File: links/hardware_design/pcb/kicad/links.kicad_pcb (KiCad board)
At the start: 2 copper layers, 19 x 108.4 mm, 55 parts, among them IC1 OPA4171, IC2 TL072PW, IC3 LM321MF, IC4 TL072PW, IC5 LM321MF, J1 PJ301_THONKICONN6, J10 PJ301_THONKICONN6, J11 PJ301_THONKICONN6, J12 PJ301_THONKICONN6, J2 PJ301_THONKICONN6, J3 PJ301_THONKICONN6, J4 PJ301_THONKICONN6, J5 PJ301_THONKICONN6, J6 PJ301_THONKICONN6, J7 PJ301_THONKICONN6, J8 PJ301_THONKICONN6, J9 PJ301_THONKICONN6

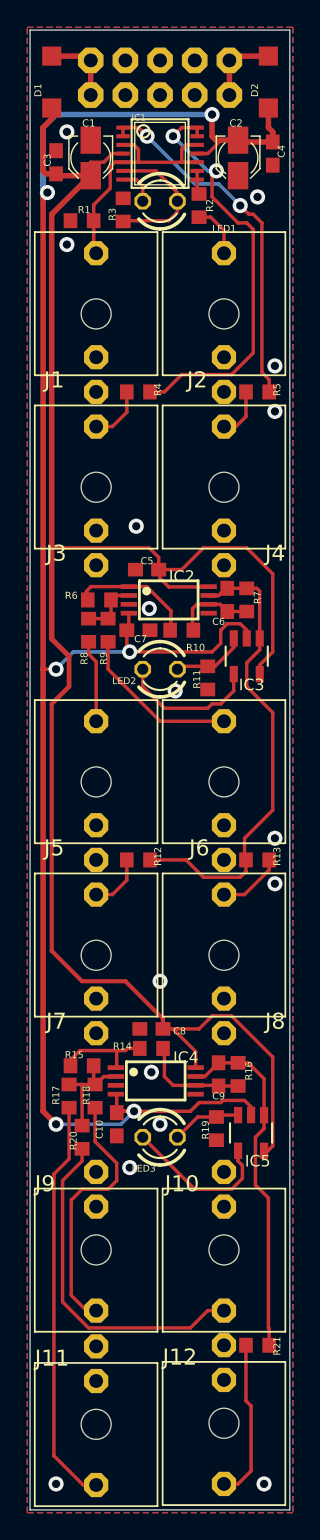
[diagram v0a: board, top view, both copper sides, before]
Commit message: links: move LEDs to left side
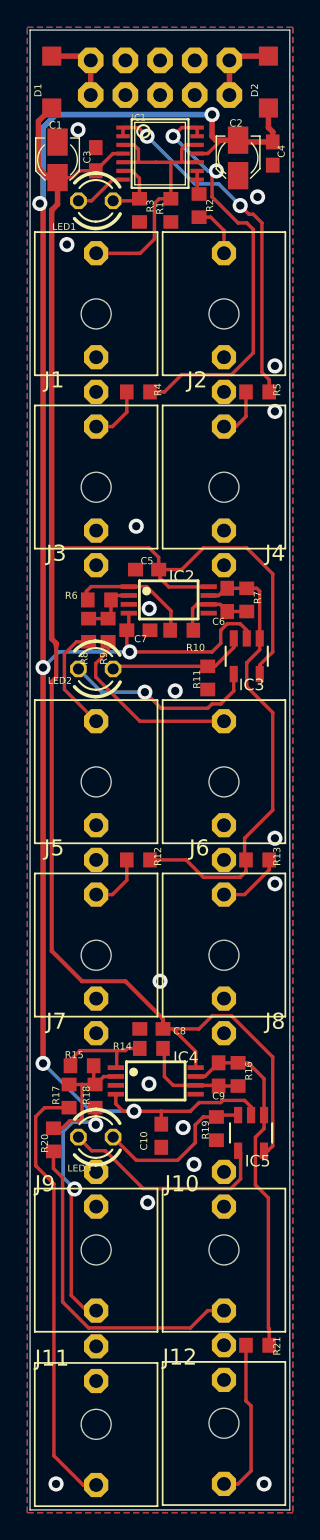
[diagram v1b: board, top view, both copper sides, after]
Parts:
- IC3, IC5: value LM321MF -> LM321?MF
- moved R1 6.55 mm to (149.3, 64.0), turned to 90 degrees
- moved LED1 4.71 mm to (143.8, 63.3)
- moved LED2 4.71 mm to (143.8, 97.6)
- moved LED3 4.71 mm to (143.8, 131.9)
- moved C10 3.37 mm to (148.6, 131.8)
- moved C3 2.92 mm to (143.8, 60.2)
- moved C1 2.44 mm to (141.0, 60.3)
- moved R20 2.10 mm to (140.7, 132.1)
- moved R3 1.19 mm to (147.0, 64.0), turned to -90 degrees
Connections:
- J12 pad P2: (no net) -> unconnected-(J12-2-PadP2)
- J2 pad P2: (no net) -> unconnected-(J2-2-PadP2)
- J3 pad P2: (no net) -> unconnected-(J3-2-PadP2)
- J4 pad P2: (no net) -> unconnected-(J4-2-PadP2)
- J7 pad P2: (no net) -> unconnected-(J7-2-PadP2)
- J8 pad P2: (no net) -> unconnected-(J8-2-PadP2)
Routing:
- net Net-(IC5--IN): track 5.37 -> 12.2 mm
- net Net-(IC1B--IN): track 10.3 -> 4.93 mm
- net Net-(IC3--IN): track 5.46 -> 10.2 mm
- net Net-(IC5-OUT): track 11.4 -> 15.9 mm
- net Net-(IC3-OUT): track 10.4 -> 14.3 mm, vias 0 -> 1
- net VEE: track 140.5 -> 136.6 mm
- net Net-(IC1A-+IN): track 17.9 -> 21.4 mm
- net Net-(J11-3): track 29.9 -> 32.1 mm
- net Net-(J5-3): track 6.05 -> 8.04 mm
- net Net-(IC4A--IN): track 8.48 -> 10.3 mm
- net VCC: track 133.8 -> 132.2 mm
- net Net-(J6-3): track 12.1 -> 13.7 mm
- net Net-(IC1B-OUT): track 2.76 -> 3.91 mm
- net Net-(J10-3): track 24.9 -> 24.4 mm
- net Net-(J9-3): track 19.2 -> 18.8 mm, vias 0 -> 2
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
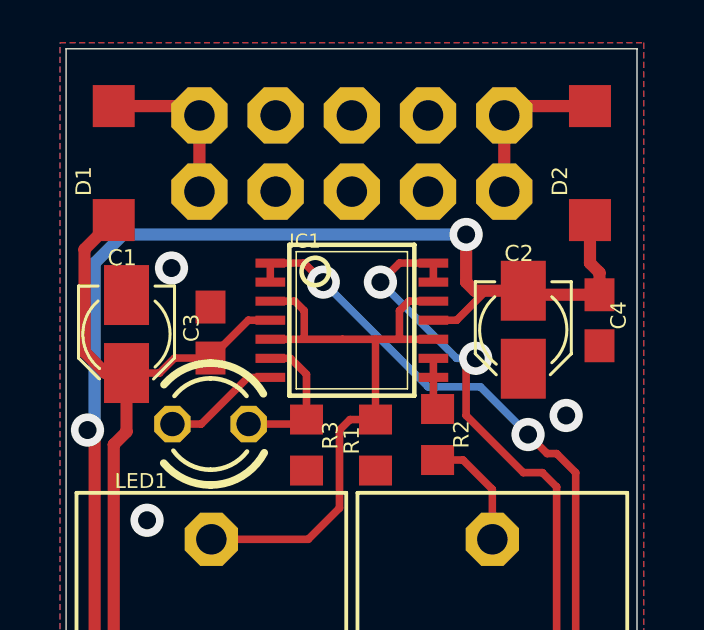
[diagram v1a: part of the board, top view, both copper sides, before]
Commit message: links: change panasonic A to 3x5.3mm footprint
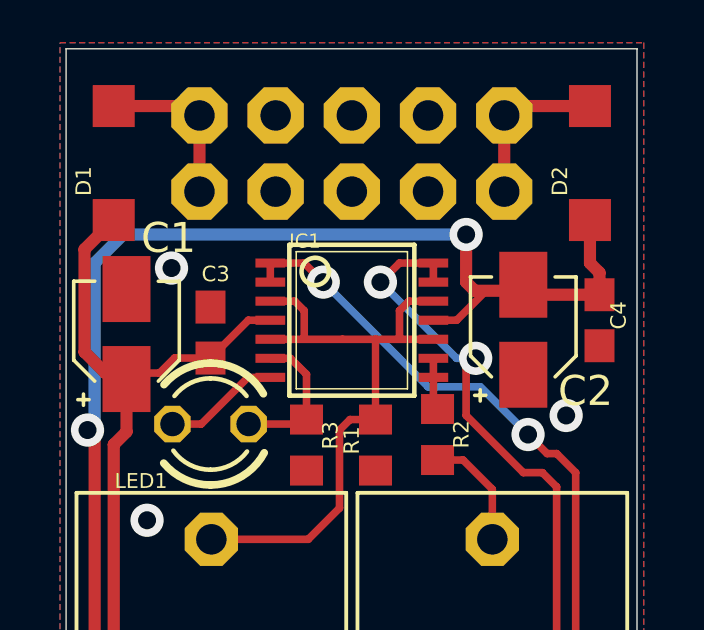
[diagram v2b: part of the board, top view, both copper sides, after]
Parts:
- C1, C2: footprint links:PANASONIC_A -> Capacitor_SMD:CP_Elec_3x5.3
- turned C1 to 90 degrees
- turned C2 to 90 degrees
